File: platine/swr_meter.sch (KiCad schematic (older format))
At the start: 16 parts, among them U1 CP0x0xx5425xNTR_Directional_C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, U2 LTC5530, U3 LM1117_SOT223, U4 STM32F030C8Tx

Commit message: HF Leiterbahnbreiten überarbeitet. HF-Teil fertig
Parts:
- C1, C5: footprint (none) -> Capacitors_SMD:C_0603
- U1: footprint (none) -> Toni:CP0603_directional_coupler
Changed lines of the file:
@@
 F 0 "U1" H 3050 2400 60  0000 C CNN
 F 1 "CP0x0xx5425xNTR_Directional_Coupler" H 3250 1900 60  0000 C CNN
-F 2 "" H 2500 2600 60  0001 C CNN
+F 2 "Toni:CP0603_directional_coupler" H 2500 2600 60  0001 C CNN
 F 3 "" H 2500 2600 60  0000 C CNN
 	1    3050 2150
@@
 F 0 "C5" H 8025 2500 50  0000 L CNN
 F 1 "100pF" H 8025 2300 50  0000 L CNN
-F 2 "" H 8038 2250 50  0001 C CNN
+F 2 "Capacitors_SMD:C_0603" H 8038 2250 50  0001 C CNN
 F 3 "" H 8000 2400 50  0000 C CNN
 	1    8000 2400
@@
 F 0 "C1" H 4675 2300 50  0000 L CNN
 F 1 "39pF" H 4675 2100 50  0000 L CNN
-F 2 "" H 4688 2050 50  0001 C CNN
+F 2 "Capacitors_SMD:C_0603" H 4688 2050 50  0001 C CNN
 F 3 "" H 4650 2200 50  0000 C CNN
 	1    4650 2200

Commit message: wiring of stm32
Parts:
- added C10, C8, C9: 100nF, Resistors_SMD:R_0402, symbol C
- added C7: 1uF, Capacitors_SMD:C_0603, symbol C
- added R5: 10R, Capacitors_SMD:C_0603, symbol R
- added U5: STM32_mmvisual_JTAG, symbol STM32_mmvisual_JTAG
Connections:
- net labels added: +3.3V, reset, tck, tdi, tdo, tms, u1_rx, u1_tx
- net labels removed: +5V
- wire segments 16 -> 35
- no-connect marks 0 -> 1
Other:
- note added: "externe clock\n7 segment\noled\n"

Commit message: routing of stm32
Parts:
- U5: footprint (none) -> Philipp:MICROMATCH-10
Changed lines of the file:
@@
 F 0 "U5" H 8400 4300 60  0000 C CNN
 F 1 "STM32_mmvisual_JTAG" H 8400 4900 60  0000 C CNN
-F 2 "" H 7450 4300 60  0001 C CNN
+F 2 "Philipp:MICROMATCH-10" H 7450 4300 60  0001 C CNN
 F 3 "" H 7450 4300 60  0000 C CNN
 	1    8400 4600

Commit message: moved micromatch. finished except oled an seven-segment display
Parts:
- added Y?: RESONATEUR, symbol RESONATEUR
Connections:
- net GND: now also Y?.2
- net at U4.3 (PC14/RCC_OSC32_IN): now also Y?.1
- net at U4.4 (PC15/RCC_OSC32_OUT): now also Y?.3
- net tdi: no longer names the net of U5.6 (TDI)
- net tdo: no longer names the net of U5.2 (TDO/SwO)
- no-connect marks 1 -> 3
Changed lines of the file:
@@
 	7850 4600 7450 4600
-Wire Wire Line
-	8950 4400 9300 4400
-Wire Wire Line
-	8950 4600 9300 4600
 Wire Wire Line
 	8950 4700 9300 4700
@@
 Text Label 7450 4600 0    60   ~ 0
 tms
-Text Label 9300 4400 0    60   ~ 0
-tdo
-Text Label 9300 4600 0    60   ~ 0
-tdi
 Text Label 9300 4700 0    60   ~ 0
 u1_rx
@@
 Text Label 1400 4100 2    60   ~ 0
 reset
-Text Label 6800 5100 0    60   ~ 0
-tdo
 Text Label 6500 6700 0    60   ~ 0
 tms
 Text Label 6500 6800 0    60   ~ 0
 tck
-Text Label 6800 5200 0    60   ~ 0
-tdi
 Text Label 6500 6400 0    60   ~ 0
 u1_rx
@@
 	6550 5500 6350 5500
 Connection ~ 6850 2150
+NoConn ~ 8950 4400
+NoConn ~ 8950 4600
+$Comp
+L RESONATEUR Y?
+U 1 1 57115A49
+P 1000 5250
+F 0 "Y?" H 1020 5450 60  0000 C CNN
+F 1 "RESONATEUR" H 1430 5050 60  0000 C CNN
+F 2 "" H 1000 5250 60  0000 C CNN
+F 3 "" H 1000 5250 60  0000 C CNN
+	1    1000 5250
+	1    0    0    -1
+$EndComp
+Wire Wire Line
+	1300 5200 1550 5200
+Wire Wire Line
+	700  5200 700  4950
+Wire Wire Line
+	700  4950 1350 4950
+Wire Wire Line
+	1350 4950 1350 5100
+Wire Wire Line
+	1350 5100 1550 5100
+$Comp
+L GND #PWR?
+U 1 1 57115E0A
+P 1000 5500
+F 0 "#PWR?" H 1000 5250 50  0001 C CNN
+F 1 "GND" H 1000 5350 50  0000 C CNN
+F 2 "" H 1000 5500 50  0000 C CNN
+F 3 "" H 1000 5500 50  0000 C CNN
+	1    1000 5500
+	1    0    0    -1
+$EndComp
 $EndSCHEMATC

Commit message: added one 7-segment display
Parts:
- added AFF?: 7SEGMENTS, symbol 7SEGMENTS
- added U?: 74HC595, symbol 74HC595
- Y1: renamed from Y?; footprint (none) -> Toni:CerOsc_3,2x1,3
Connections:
- net +3V3: now also AFF?.3 (C.A.), AFF?.8 (C.A.)
- net GND: now also U?.8 (GND)
- new net VCC: U?.16 (VCC)
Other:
- note added: "7 segment\noled\n"
- note removed: "externe clock\n7 segment\noled\n"
- moved on the sheet: C2, C3, C5, C6, U3, U5

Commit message: work on 7-segment display
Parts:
- added AFF2: 7SEGMENTS, Housings_DIP:DIP-10_W7.62mm, symbol 7SEGMENTS
- added RP1, RP2, RP3, RP4: R_PACK4, Toni:R_array_4, symbol R_PACK4
- added U7: 74HC595, Housings_SOIC:SOIC-16_3.9x9.9mm_Pitch1.27mm, symbol 74HC595
- AFF1: renamed from AFF?; footprint (none) -> Housings_DIP:DIP-10_W7.62mm
- U6: renamed from U?; footprint (none) -> Housings_SOIC:SOIC-16_3.9x9.9mm_Pitch1.27mm
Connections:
- net VCC is gone; now on net +3V3: U6.16 (VCC)
- net +3V3: now also AFF2.3 (C.A.), AFF2.8 (C.A.), U7.16 (VCC)
- net GND: now also U7.8 (GND)
- net at AFF1.1 (e): now also RP2.5 (R4)
- net at AFF1.10 (g): now also RP1.8 (R1)
- net at AFF1.2 (d): now also RP2.6 (R3)
- net at AFF1.4 (c): now also RP2.7 (R2)
- net at AFF1.5 (DP): now also RP2.8 (R1)
- net at AFF1.6 (b): now also RP1.5 (R4)
- net at AFF1.7 (a): now also RP1.6 (R3)
- net at AFF1.9 (f): now also RP1.7 (R2)
- net at U6.1 (QB): now also RP1.2 (P2)
- net at U6.15 (QA): now also RP1.1 (P1)
- net at U6.2 (QC): now also RP1.3 (P3)
- net at U6.3 (QD): now also RP1.4 (P4)
- net at U6.4 (QE): now also RP2.1 (P1)
- net at U6.5 (QF): now also RP2.2 (P2)
- net at U6.6 (QG): now also RP2.3 (P3)
- net at U6.7 (QH): now also RP2.4 (P4)
- net at U6.9 (~QH): now also U7.14 (SER)
- new net: AFF2.1 (e), RP4.5 (R4)
- new net: AFF2.10 (g), RP3.8 (R1)
- new net: AFF2.2 (d), RP4.6 (R3)
- new net: AFF2.4 (c), RP4.7 (R2)
- new net: AFF2.5 (DP), RP4.8 (R1)
- new net: AFF2.6 (b), RP3.5 (R4)
- new net: AFF2.7 (a), RP3.6 (R3)
- new net: AFF2.9 (f), RP3.7 (R2)
- new net: RP3.2 (P2), U7.1 (QB)
- new net: RP3.1 (P1), U7.15 (QA)
- new net: RP3.3 (P3), U7.2 (QC)
- new net: RP3.4 (P4), U7.3 (QD)
- new net: RP4.1 (P1), U7.4 (QE)
- new net: RP4.2 (P2), U7.5 (QF)
- new net: RP4.3 (P3), U7.6 (QG)
- new net: RP4.4 (P4), U7.7 (QH)
- no-connect marks 3 -> 4
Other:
- moved on the sheet: AFF1, U6

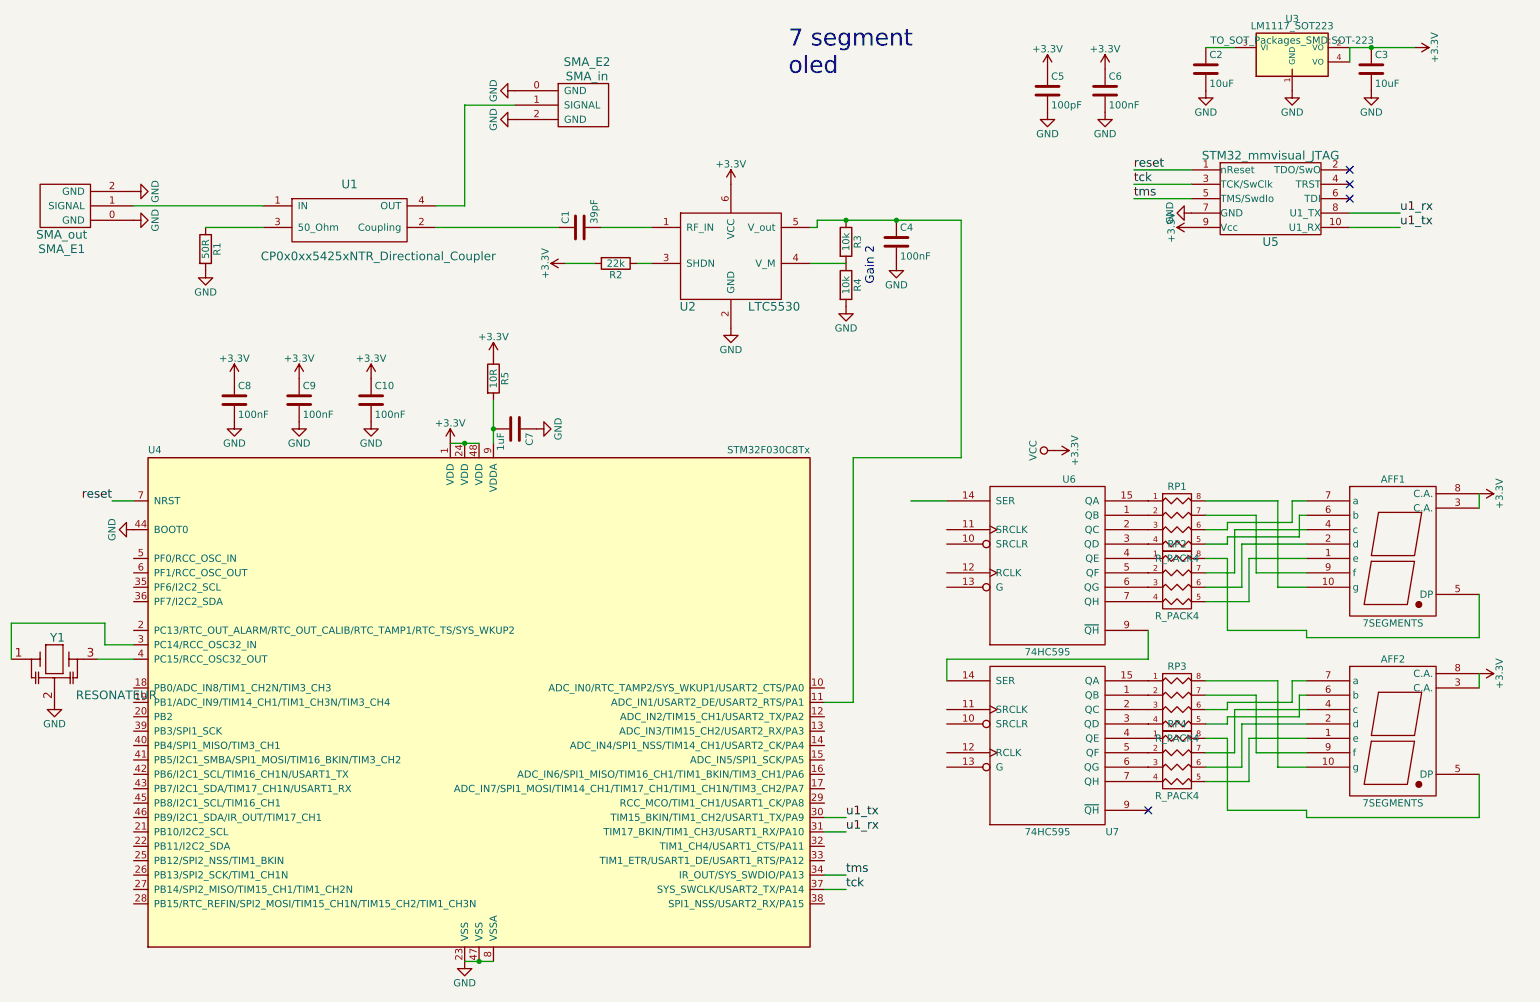
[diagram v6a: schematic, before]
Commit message: 7segments angeschlossen und resonator berichtigt
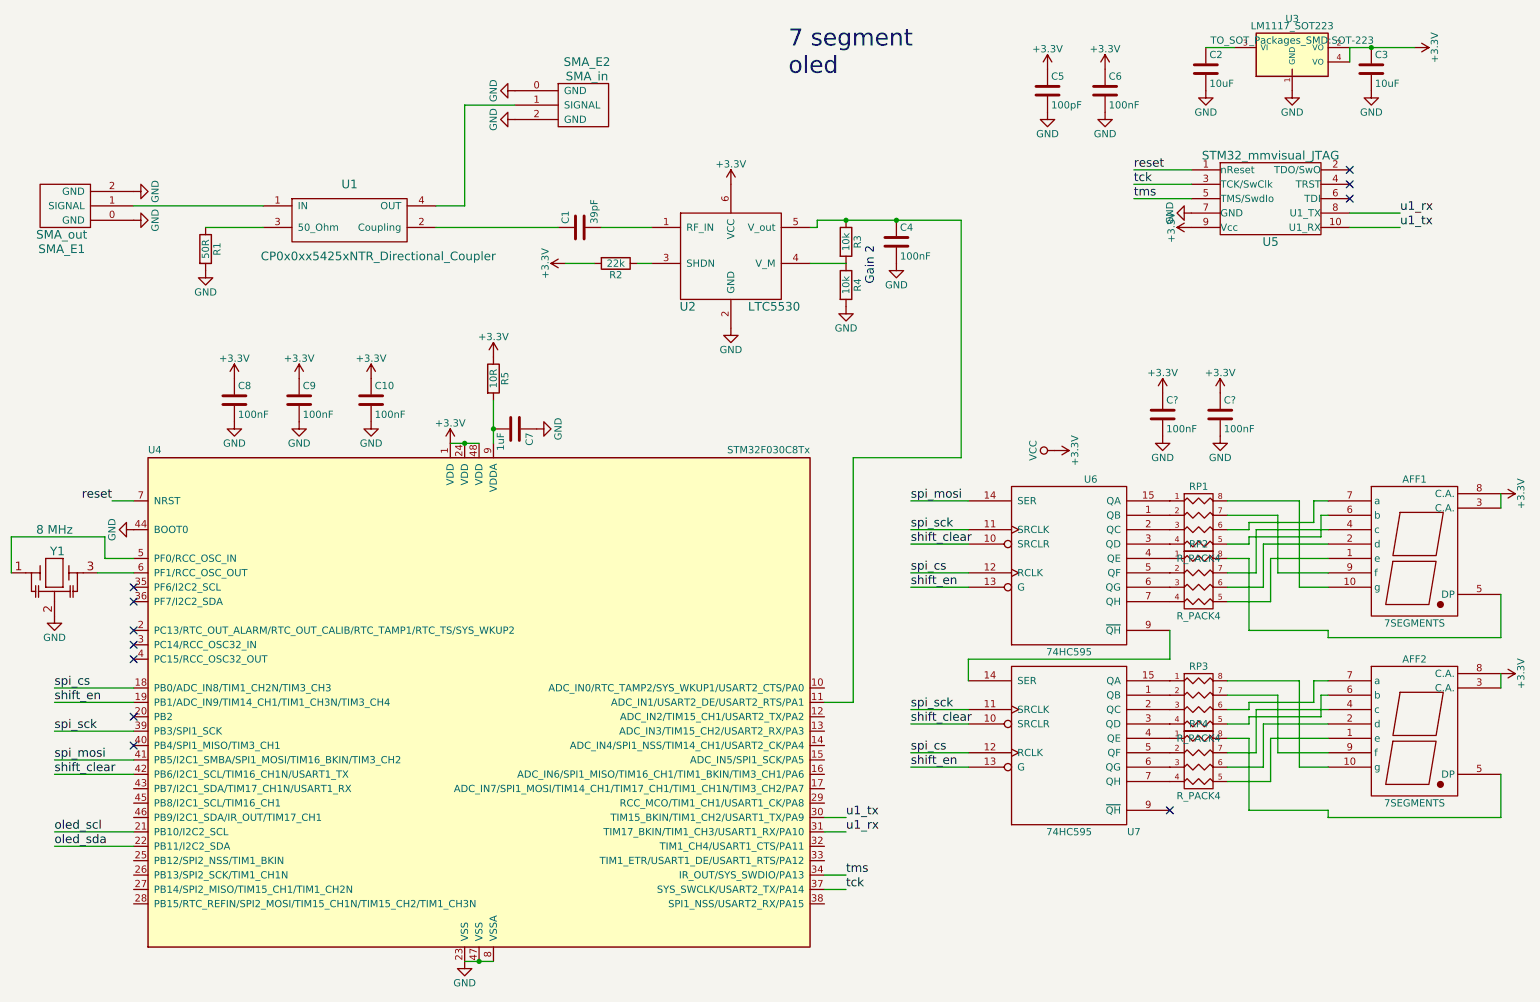
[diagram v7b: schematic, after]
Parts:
- added C? (x2): 100nF, Resistors_SMD:R_0402, symbol C
- Y1: value RESONATEUR -> 8 MHz
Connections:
- net +3V3: now also C?.1, C?.1
- net GND: now also C?.2, C?.2
- net spi_cs: now reaches U4.18 (PB0/ADC_IN8/TIM1_CH2N/TIM3_CH3)
- net spi_cs: now also U6.12 (RCLK), U7.12 (RCLK)
- net shift_en: now reaches U4.19 (PB1/ADC_IN9/TIM14_CH1/TIM1_CH3N/TIM3_CH4)
- net shift_en: now also U6.13 (G), U7.13 (G)
- net oled_scl: now reaches U4.21 (PB10/I2C2_SCL)
- net oled_sda: now reaches U4.22 (PB11/I2C2_SDA)
- net at U4.3 (PC14/RCC_OSC32_IN): no longer Y1.1
- net spi_sck: now reaches U4.39 (PB3/SPI1_SCK)
- net spi_sck: now also U6.11 (SRCLK), U7.11 (SRCLK)
- net at U4.4 (PC15/RCC_OSC32_OUT): no longer Y1.3
- net spi_mosi: now reaches U4.41 (PB5/I2C1_SMBA/SPI1_MOSI/TIM16_BKIN/TIM3_CH2)
- net spi_mosi: now also U6.14 (SER)
- net shift_clear: now reaches U4.42 (PB6/I2C1_SCL/TIM16_CH1N/USART1_TX)
- net shift_clear: now also U6.10 (SRCLR), U7.10 (SRCLR)
- net at U4.5 (PF0/RCC_OSC_IN): now also Y1.1
- net at U4.6 (PF1/RCC_OSC_OUT): now also Y1.3
- no-connect marks 4 -> 11
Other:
- moved on the sheet: AFF1, AFF2, RP1, RP2, RP3, RP4, U6, U7, Y1

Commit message: schematic complete, pcb complete, drc ok
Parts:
- added P1: Oled, Pin_Headers:Pin_Header_Straight_1x04, symbol CONN_01X04
- added P2: Vin, Pin_Headers:Pin_Header_Straight_1x02, symbol CONN_01X02
- gave numbers to parts that had none: 2
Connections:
- net +3V3: now also P1.2 (P2)
- net GND: now also P1.1 (P1), P2.1 (P1)
- net oled_scl: now also P1.3 (P3)
- net oled_sda: now also P1.4 (P4)
- net at C2.1, U3.3 (VI): now also P2.2 (P2)
- no-connect marks 11 -> 29
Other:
- note removed: "7 segment\noled\n"
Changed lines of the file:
@@
 LIBS:cp0x0xx5425xntr_directional_coupler
 LIBS:ltc5530
+LIBS:toni
 LIBS:lmh2110
 LIBS:stm32
+LIBS:prog_sockets
 LIBS:swr_meter-cache
 EELAYER 25 0
@@
 $EndComp
 Wire Wire Line
-	9200 950  9000 950
+	8850 950  9200 950
 $Comp
 L LM1117_SOT223 U3
@@
 	0    1    1    0
 $EndComp
-Text Notes 6100 1150 0    118  ~ 0
-7 segment\noled\n
 $Comp
 L +3.3V #PWR015
@@
 P 3750 3700
 F 0 "#PWR020" H 3750 3550 50  0001 C CNN
-F 1 "+3.3V" H 3750 3840 50  0000 C CNN
+F 1 "+3.3V" H 3650 3850 50  0000 C CNN
 F 2 "" H 3750 3700 50  0000 C CNN
 F 3 "" H 3750 3700 50  0000 C CNN
@@
 shift_en
 $Comp
-L C C?
+L C C11
 U 1 1 57117606
 P 8700 3500
-F 0 "C?" H 8725 3600 50  0000 L CNN
+F 0 "C11" H 8725 3600 50  0000 L CNN
 F 1 "100nF" H 8725 3400 50  0000 L CNN
 F 2 "Resistors_SMD:R_0402" H 8738 3350 50  0001 C CNN
@@
 $EndComp
 $Comp
-L GND #PWR?
+L GND #PWR037
 U 1 1 5711760C
 P 8700 3650
-F 0 "#PWR?" H 8700 3400 50  0001 C CNN
+F 0 "#PWR037" H 8700 3400 50  0001 C CNN
 F 1 "GND" H 8700 3500 50  0000 C CNN
 F 2 "" H 8700 3650 50  0000 C CNN
@@
 $EndComp
 $Comp
-L +3.3V #PWR?
+L +3.3V #PWR038
 U 1 1 57117612
 P 8700 3350
-F 0 "#PWR?" H 8700 3200 50  0001 C CNN
+F 0 "#PWR038" H 8700 3200 50  0001 C CNN
 F 1 "+3.3V" H 8700 3490 50  0000 C CNN
 F 2 "" H 8700 3350 50  0000 C CNN
@@
 $EndComp
 $Comp
-L C C?
+L C C12
 U 1 1 5711767E
 P 9100 3500
-F 0 "C?" H 9125 3600 50  0000 L CNN
+F 0 "C12" H 9125 3600 50  0000 L CNN
 F 1 "100nF" H 9125 3400 50  0000 L CNN
 F 2 "Resistors_SMD:R_0402" H 9138 3350 50  0001 C CNN
@@
 $EndComp
 $Comp
-L GND #PWR?
+L GND #PWR039
 U 1 1 57117684
 P 9100 3650
-F 0 "#PWR?" H 9100 3400 50  0001 C CNN
+F 0 "#PWR039" H 9100 3400 50  0001 C CNN
 F 1 "GND" H 9100 3500 50  0000 C CNN
 F 2 "" H 9100 3650 50  0000 C CNN
@@
 $EndComp
 $Comp
-L +3.3V #PWR?
+L +3.3V #PWR040
 U 1 1 5711768A
 P 9100 3350
-F 0 "#PWR?" H 9100 3200 50  0001 C CNN
+F 0 "#PWR040" H 9100 3200 50  0001 C CNN
 F 1 "+3.3V" H 9100 3490 50  0000 C CNN
 F 2 "" H 9100 3350 50  0000 C CNN
@@
 NoConn ~ 1550 5800
 NoConn ~ 1550 5600
+$Comp
+L CONN_01X04 P1
+U 1 1 571170AA
+P 8450 2750
+F 0 "P1" H 8450 3000 50  0000 C CNN
+F 1 "Oled" V 8550 2750 50  0000 C CNN
+F 2 "Pin_Headers:Pin_Header_Straight_1x04" H 8450 2750 50  0001 C CNN
+F 3 "" H 8450 2750 50  0000 C CNN
+	1    8450 2750
+	1    0    0    -1
+$EndComp
+$Comp
+L GND #PWR041
+U 1 1 571172A6
+P 8250 2600
+F 0 "#PWR041" H 8250 2350 50  0001 C CNN
+F 1 "GND" H 8250 2450 50  0000 C CNN
+F 2 "" H 8250 2600 50  0000 C CNN
+F 3 "" H 8250 2600 50  0000 C CNN
+	1    8250 2600
+	0    1    1    0
+$EndComp
+$Comp
+L +3.3V #PWR042
+U 1 1 5711731E
+P 8250 2700
+F 0 "#PWR042" H 8250 2550 50  0001 C CNN
+F 1 "+3.3V" H 8250 2840 50  0000 C CNN
+F 2 "" H 8250 2700 50  0000 C CNN
+F 3 "" H 8250 2700 50  0000 C CNN
+	1    8250 2700
+	0    -1   -1   0
+$EndComp
+Text Label 8000 2800 2    60   ~ 0
+oled_scl
+Text Label 8000 2900 2    60   ~ 0
+oled_sda
+Wire Wire Line
+	8250 2800 8000 2800
+Wire Wire Line
+	8000 2900 8250 2900
+NoConn ~ 1550 6900
+NoConn ~ 1550 6800
+NoConn ~ 1550 6700
+NoConn ~ 1550 6600
+NoConn ~ 1550 6300
+NoConn ~ 1550 6200
+NoConn ~ 1550 6100
+NoConn ~ 6350 6900
+NoConn ~ 6350 6600
+NoConn ~ 6350 6500
+NoConn ~ 6350 6200
+NoConn ~ 6350 6100
+NoConn ~ 6350 6000
+NoConn ~ 6350 5400
+NoConn ~ 6350 5600
+NoConn ~ 6350 5700
+NoConn ~ 6350 5800
+NoConn ~ 6350 5900
+$Comp
+L PWR_FLAG #FLG043
+U 1 1 57118079
+P 7950 3750
+F 0 "#FLG043" H 7950 3845 50  0001 C CNN
+F 1 "PWR_FLAG" H 7950 3930 50  0000 C CNN
+F 2 "" H 7950 3750 50  0000 C CNN
+F 3 "" H 7950 3750 50  0000 C CNN
+	1    7950 3750
+	1    0    0    -1
+$EndComp
+$Comp
+L PWR_FLAG #FLG044
+U 1 1 57118225
+P 9000 950
+F 0 "#FLG044" H 9000 1045 50  0001 C CNN
+F 1 "PWR_FLAG" H 9000 1130 50  0000 C CNN
+F 2 "" H 9000 950 50  0000 C CNN
+F 3 "" H 9000 950 50  0000 C CNN
+	1    9000 950
+	1    0    0    -1
+$EndComp
+$Comp
+L PWR_FLAG #FLG045
+U 1 1 5711894C
+P 4050 3400
+F 0 "#FLG045" H 4050 3495 50  0001 C CNN
+F 1 "PWR_FLAG" H 4050 3580 50  0000 C CNN
+F 2 "" H 4050 3400 50  0000 C CNN
+F 3 "" H 4050 3400 50  0000 C CNN
+	1    4050 3400
+	0    -1   -1   0
+$EndComp
+$Comp
+L CONN_01X02 P2
+U 1 1 57119187
+P 8650 1000
+F 0 "P2" H 8650 1150 50  0000 C CNN
+F 1 "Vin" V 8750 1000 50  0000 C CNN
+F 2 "Pin_Headers:Pin_Header_Straight_1x02" H 8650 1000 50  0001 C CNN
+F 3 "" H 8650 1000 50  0000 C CNN
+	1    8650 1000
+	-1   0    0    1
+$EndComp
+Connection ~ 9000 950
+Wire Wire Line
+	8850 1050 8850 1250
+Wire Wire Line
+	8850 1250 9000 1250
 $EndSCHEMATC
